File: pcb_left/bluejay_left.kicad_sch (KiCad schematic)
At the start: 82 parts, among them J1 SJ-43514, U1 ATmega328P-PU, Y1 16MHz

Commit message: Produce test gerber files
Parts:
- removed J?: Screw_Terminal_01x04, symbol Connector:Screw_Terminal_01x04
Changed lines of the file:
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@@
     (pin "2")
-  )
-  (symbol (lib_id "Connector:Screw_Terminal_01x04") (at 144.78 156.21 90) (unit 1)
-    (in_bom yes) (on_board yes) (fields_autoplaced)
-    (property "Reference" "J?" (id 0) (at 146.05 149.86 90))
-    (property "Value" "Screw_Terminal_01x04" (id 1) (at 146.05 152.4 90))
-    (property "Footprint" "" (id 2) (at 144.78 156.21 0)
-      (effects (font (size 1.27 1.27)) hide)
-    )
-    (property "Datasheet" "~" (id 3) (at 144.78 156.21 0)
-      (effects (font (size 1.27 1.27)) hide)
-    )
-    (pin "1")
-    (pin "2")
-    (pin "3")
-    (pin "4")
   )
   (symbol (lib_id "Diode_AKL:1N4148") (at 138.43 86.36 180) (unit 1)
@@
       (reference "J1") (unit 1) (value "SJ-43514") (footprint "BlueJay footprints:CUI_SJ-43514")
     )
-    (path "/1447b0b5-ab38-407e-b41f-aa727794d4da"
-      (reference "J?") (unit 1) (value "Screw_Terminal_01x04") (footprint "")
-    )
     (path "/31642483-9c10-4ba0-a4b2-91eb418caf17"

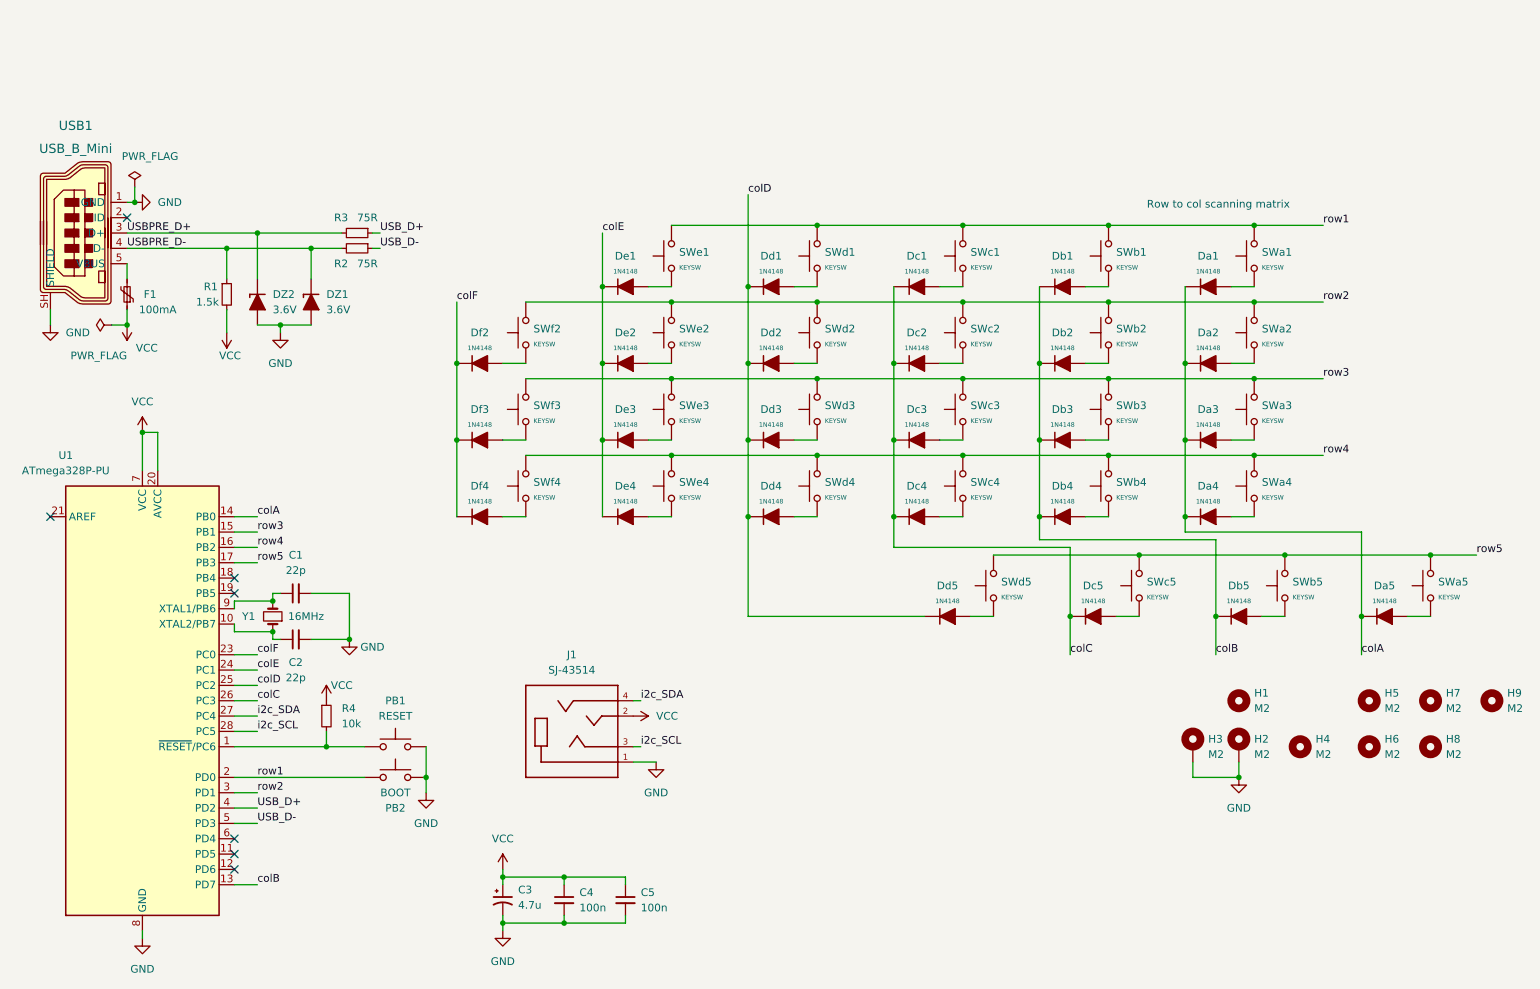
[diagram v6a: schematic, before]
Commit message: Update schematics in preparation for review
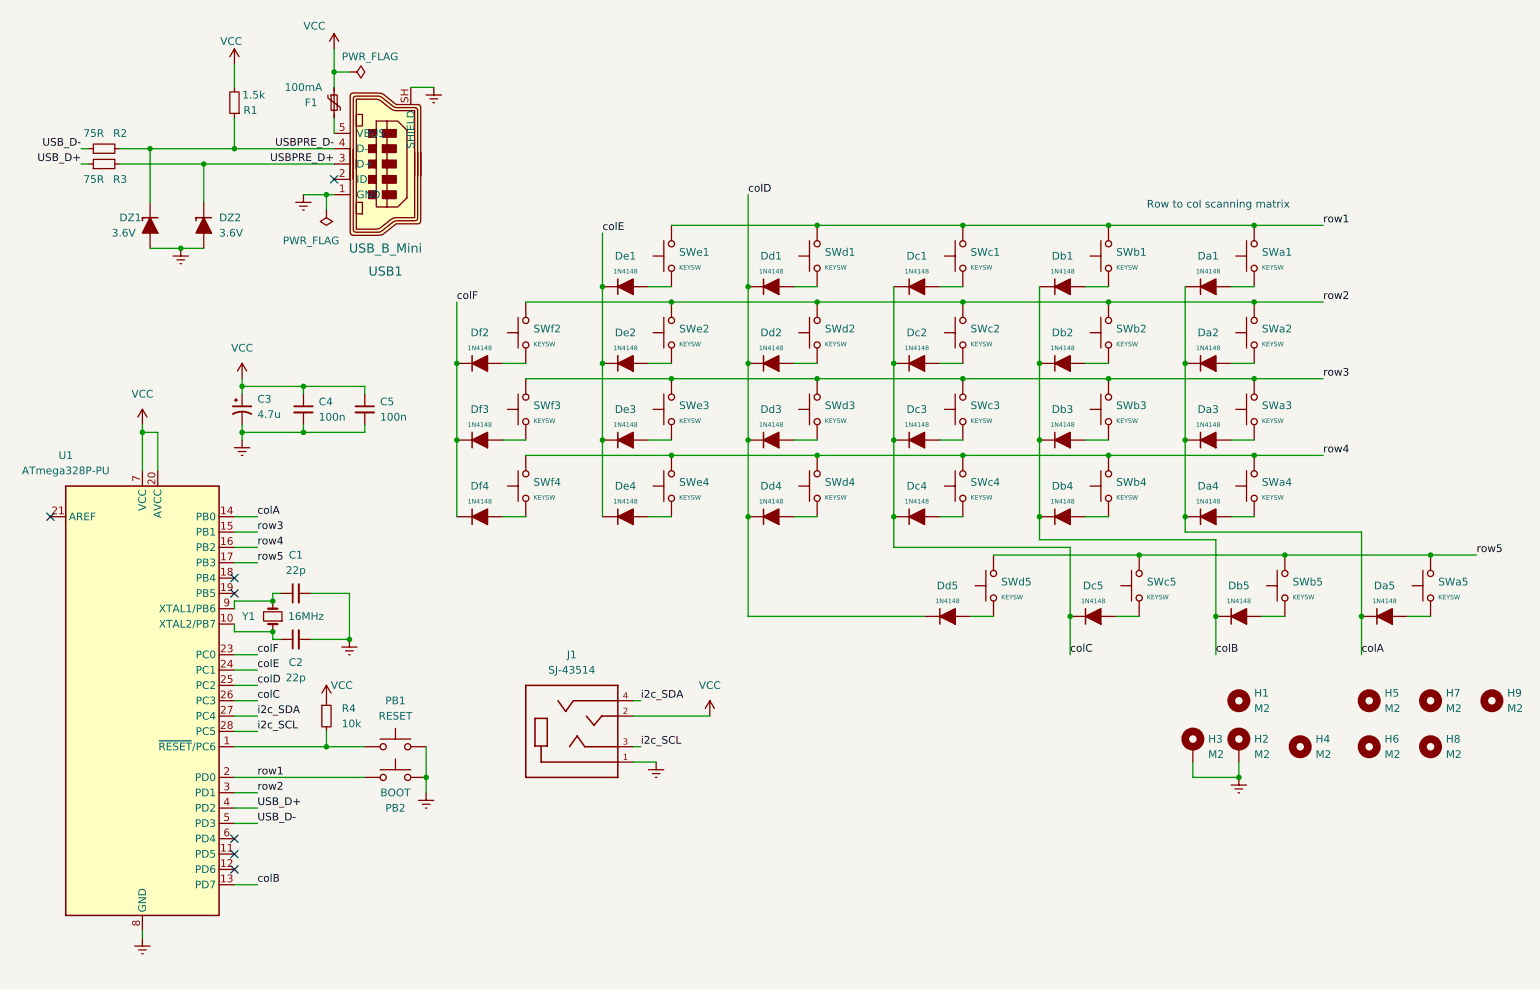
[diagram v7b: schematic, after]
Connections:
- net GND renamed Earth
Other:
- moved on the sheet: C3, C4, C5, DZ1, DZ2, F1, R1, R2, R3, USB1

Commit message: Fine tuning of schematics and pcbs in prep for review
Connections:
- net Earth renamed GND
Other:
- note added: "Low speed usb"
- note added: "TRRS jack"
- note added: "Total bypass caps (both sides combined) = 9.7uF"
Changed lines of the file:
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@@
     (stroke (width 0) (type default) (color 0 0 0 0))
+  )
+  (text "Low speed usb" (at 39.37 43.18 0)
+    (effects (font (size 1.27 1.27)) (justify left bottom))
+  )
+  (text "Total bypass caps (both sides combined) = 9.7uF" (at 30.48 92.71 0)
+    (effects (font (size 1.27 1.27)) (justify left bottom))
+  )
+  (text "TRRS jack" (at 105.41 172.72 0)
+    (effects (font (size 1.27 1.27)) (justify left bottom))
   )
   (text "Row to col scanning matrix" (at 200.66 73.66 0)
@@
     (pin "2")
   )
-  (symbol (lib_id "power:Earth") (at 40.64 80.01 0) (unit 1)
+  (symbol (lib_id "power:GND") (at 40.64 80.01 0) (unit 1)
     (in_bom yes) (on_board yes) (fields_autoplaced)
     (property "Reference" "#PWR0106" (id 0) (at 40.64 86.36 0)
       (effects (font (size 1.27 1.27)) hide)
     )
-    (property "Value" "Earth" (id 1) (at 40.64 85.09 0)
+    (property "Value" "GND" (id 1) (at 40.64 83.82 0)
       (effects (font (size 1.27 1.27)) hide)
     )
@@
     (pin "2")
   )
-  (symbol (lib_id "power:Earth") (at 34.29 194.31 0) (unit 1)
+  (symbol (lib_id "power:GND") (at 34.29 194.31 0) (unit 1)
     (in_bom yes) (on_board yes) (fields_autoplaced)
     (property "Reference" "#PWR0108" (id 0) (at 34.29 200.66 0)
       (effects (font (size 1.27 1.27)) hide)
     )
-    (property "Value" "Earth" (id 1) (at 34.29 199.39 0)
+    (property "Value" "GND" (id 1) (at 34.29 198.12 0)
       (effects (font (size 1.27 1.27)) hide)
     )
@@
     (pin "1")
   )
-  (symbol (lib_id "power:Earth") (at 50.8 111.76 0) (unit 1)
+  (symbol (lib_id "power:GND") (at 50.8 111.76 0) (unit 1)
     (in_bom yes) (on_board yes) (fields_autoplaced)
     (property "Reference" "#PWR0102" (id 0) (at 50.8 118.11 0)
       (effects (font (size 1.27 1.27)) hide)
     )
-    (property "Value" "Earth" (id 1) (at 50.8 116.84 0)
+    (property "Value" "GND" (id 1) (at 50.8 115.57 0)
       (effects (font (size 1.27 1.27)) hide)
     )
@@
     (pin "2")
   )
-  (symbol (lib_id "power:Earth") (at 119.38 165.1 0) (unit 1)
+  (symbol (lib_id "power:GND") (at 119.38 165.1 0) (unit 1)
     (in_bom yes) (on_board yes) (fields_autoplaced)
     (property "Reference" "#PWR0113" (id 0) (at 119.38 171.45 0)
       (effects (font (size 1.27 1.27)) hide)
     )
-    (property "Value" "Earth" (id 1) (at 119.38 170.18 0)
+    (property "Value" "GND" (id 1) (at 119.38 168.91 0)
       (effects (font (size 1.27 1.27)) hide)
     )
@@
     (pin "1")
   )
-  (symbol (lib_id "power:Earth") (at 60.96 71.12 0) (unit 1)
+  (symbol (lib_id "power:GND") (at 60.96 71.12 0) (unit 1)
     (in_bom yes) (on_board yes)
     (property "Reference" "#PWR0103" (id 0) (at 60.96 77.47 0)
       (effects (font (size 1.27 1.27)) hide)
     )
-    (property "Value" "Earth" (id 1) (at 60.96 74.93 90)
-      (effects (font (size 1.27 1.27)) (justify right) hide)
-    )
+    (property "Value" "GND" (id 1) (at 60.96 74.93 0))
     (property "Footprint" "" (id 2) (at 60.96 71.12 0)
       (effects (font (size 1.27 1.27)) hide)
@@
     (pin "2")
   )
-  (symbol (lib_id "power:Earth") (at 81.28 170.18 0) (unit 1)
+  (symbol (lib_id "power:GND") (at 81.28 170.18 0) (unit 1)
     (in_bom yes) (on_board yes) (fields_autoplaced)
     (property "Reference" "#PWR0111" (id 0) (at 81.28 176.53 0)
       (effects (font (size 1.27 1.27)) hide)
     )
-    (property "Value" "Earth" (id 1) (at 81.28 175.26 0)
+    (property "Value" "GND" (id 1) (at 81.28 173.99 0)
       (effects (font (size 1.27 1.27)) hide)
     )
@@
     (pin "2")
   )
-  (symbol (lib_id "power:Earth") (at 215.9 167.64 0) (unit 1)
+  (symbol (lib_id "power:GND") (at 215.9 167.64 0) (unit 1)
     (in_bom yes) (on_board yes) (fields_autoplaced)
     (property "Reference" "#PWR0115" (id 0) (at 215.9 173.99 0)
       (effects (font (size 1.27 1.27)) hide)
     )
-    (property "Value" "Earth" (id 1) (at 215.9 172.72 0)
+    (property "Value" "GND" (id 1) (at 215.9 171.45 0)
       (effects (font (size 1.27 1.27)) hide)
     )
@@
     (pin "2")
   )
-  (symbol (lib_id "power:Earth") (at 82.55 53.34 0) (unit 1)
+  (symbol (lib_id "power:GND") (at 82.55 53.34 0) (unit 1)
     (in_bom yes) (on_board yes) (fields_autoplaced)
     (property "Reference" "#PWR0114" (id 0) (at 82.55 59.69 0)
       (effects (font (size 1.27 1.27)) hide)
     )
-    (property "Value" "Earth" (id 1) (at 85.09 54.6099 0)
-      (effects (font (size 1.27 1.27)) (justify left) hide)
-    )
+    (property "Value" "GND" (id 1) (at 82.55 57.15 0))
     (property "Footprint" "" (id 2) (at 82.55 53.34 0)
       (effects (font (size 1.27 1.27)) hide)
@@
     (pin "2")
   )
-  (symbol (lib_id "power:Earth") (at 68.58 144.78 0) (unit 1)
+  (symbol (lib_id "power:GND") (at 68.58 144.78 0) (unit 1)
     (in_bom yes) (on_board yes)
     (property "Reference" "#PWR0109" (id 0) (at 68.58 151.13 0)
       (effects (font (size 1.27 1.27)) hide)
     )
-    (property "Value" "Earth" (id 1) (at 72.39 146.05 0)
+    (property "Value" "GND" (id 1) (at 68.58 148.59 0)
       (effects (font (size 1.27 1.27)) hide)
     )
@@
     )
     (path "/4a764b71-3549-41f2-956b-5e0c88d08a53"
-      (reference "#PWR0102") (unit 1) (value "Earth") (footprint "")
+      (reference "#PWR0102") (unit 1) (value "GND") (footprint "")
     )
     (path "/82c22113-2e14-4d6e-aa2b-b87dfa527f5e"
-      (reference "#PWR0103") (unit 1) (value "Earth") (footprint "")
+      (reference "#PWR0103") (unit 1) (value "GND") (footprint "")
     )
     (path "/dbad4ed4-d45c-4d59-94e2-f9535f75f8ab"
@@
     )
     (path "/2a991569-6da2-4bc1-81c0-7d9a648519d5"
-      (reference "#PWR0106") (unit 1) (value "Earth") (footprint "")
+      (reference "#PWR0106") (unit 1) (value "GND") (footprint "")
     )
     (path "/4b08dc79-71a1-49aa-9331-a900da4ecc63"
@@
     )
     (path "/35c4581b-ad58-4c6a-b9b5-a7da8d3ffce0"
-      (reference "#PWR0108") (unit 1) (value "Earth") (footprint "")
+      (reference "#PWR0108") (unit 1) (value "GND") (footprint "")
     )
     (path "/ef505780-efbb-4972-90a1-9efb3e3977fd"
-      (reference "#PWR0109") (unit 1) (value "Earth") (footprint "")
+      (reference "#PWR0109") (unit 1) (value "GND") (footprint "")
     )
     (path "/b09d4092-0c6d-4b88-bd07-7b6acc0ac6d0"
@@
     )
     (path "/89611a16-088f-4ab1-9e87-35529a119b1a"
-      (reference "#PWR0111") (unit 1) (value "Earth") (footprint "")
+      (reference "#PWR0111") (unit 1) (value "GND") (footprint "")
     )
     (path "/248864a2-91ef-4d14-87e7-7b68a9c3eb73"
@@
     )
     (path "/5db823f5-1028-4c25-9628-3c5bc8f81679"
-      (reference "#PWR0113") (unit 1) (value "Earth") (footprint "")
+      (reference "#PWR0113") (unit 1) (value "GND") (footprint "")
     )
     (path "/d6b19f23-8e97-4cc2-a56b-2d95cd97c2e8"
-      (reference "#PWR0114") (unit 1) (value "Earth") (footprint "")
+      (reference "#PWR0114") (unit 1) (value "GND") (footprint "")
     )
     (path "/aa799aa4-0b77-4e69-bd3a-b95b04823f1a"
-      (reference "#PWR0115") (unit 1) (value "Earth") (footprint "")
+      (reference "#PWR0115") (unit 1) (value "GND") (footprint "")
     )
     (path "/709a6874-5923-446e-9322-a60e23d13f71"
